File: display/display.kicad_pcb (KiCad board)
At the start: 2 copper layers, 35.8 x 14 mm, 2 parts, among them P1 51281-1694, P2 CONN_14

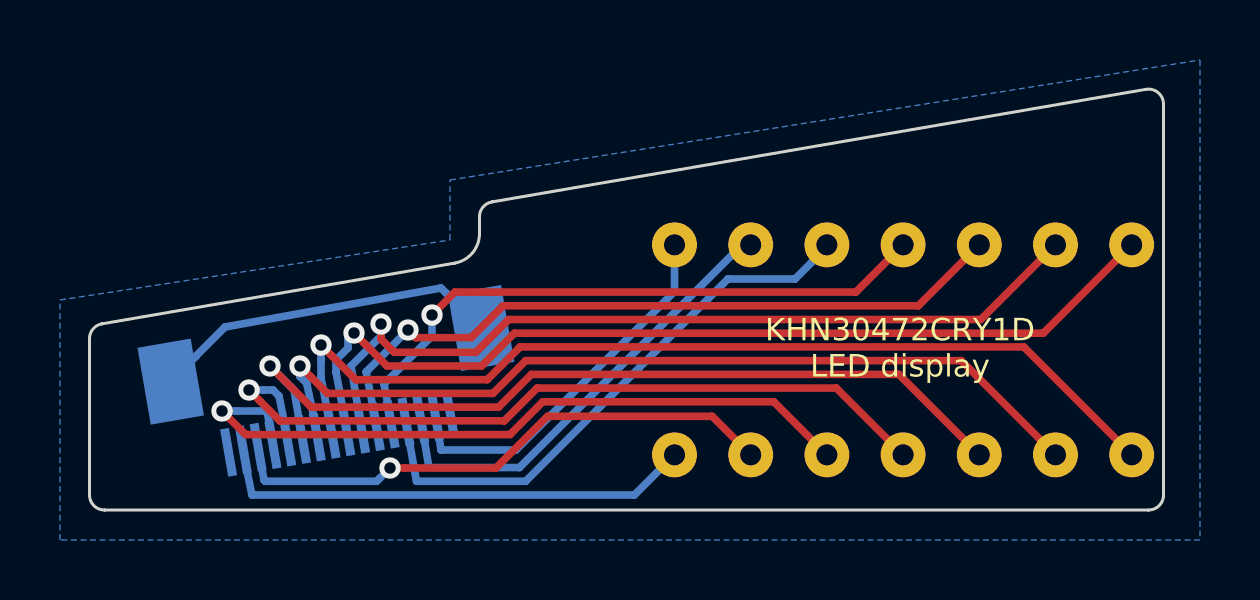
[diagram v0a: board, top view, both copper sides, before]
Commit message: Update FFC connector on the display board.
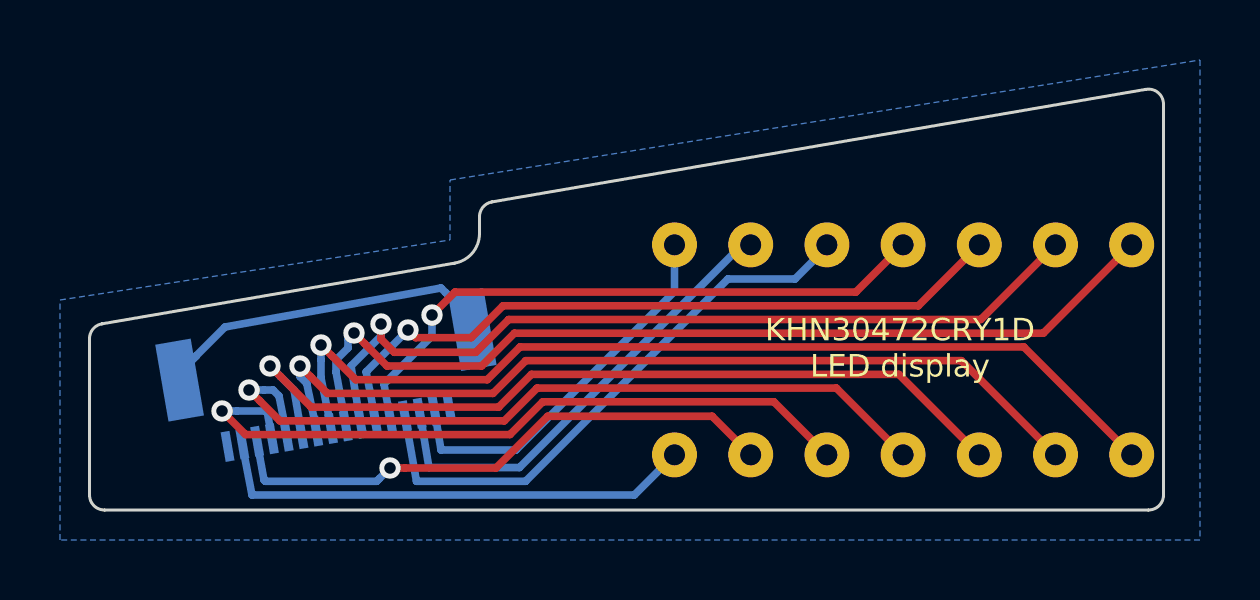
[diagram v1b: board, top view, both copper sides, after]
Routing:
- net /SW9: track 25.0 -> 23.7 mm
- net /CS1: track 33.1 -> 31.8 mm
- net /SW11: track 29.1 -> 28.0 mm
- net /SW7: track 15.5 -> 16.0 mm
- net /CS7: track 15.1 -> 15.6 mm

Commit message: Bump version to 3.1.0
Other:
- board text added: "PCB ID: uhk60v2_display_3.1.0"
- board text removed: "PCB ID: uhk60v2_display_3.0.0"
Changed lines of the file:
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@@
   (title_block
     (title "UHK 60 v2 - LED Display Board")
-    (rev 3.0.0)
+    (rev 3.1.0)
     (company "Ultimate Gadget Laboratories Kft.")
   )
@@
   )
   (setup
-    (last_trace_width 0.254)
+    (last_trace_width 0.3048)
     (user_trace_width 0.2032)
     (user_trace_width 0.254)
@@
   (gr_line (start 135.27385 98.805944) (end 157.073845 95.052999) (angle 90) (layer Edge.Cuts) (width 0.1))
   (gr_arc (start 122.358734 108.576078) (end 121.858673 108.576147) (angle -89.94233769) (layer Edge.Cuts) (width 0.1))
-  (gr_text "PCB ID: uhk60v2_display_3.0.0" (at 157.475 103.775) (layer B.SilkS)
+  (gr_text "PCB ID: uhk60v2_display_3.1.0" (at 157.475 103.775) (layer B.SilkS)
     (effects (font (size 0.75 0.75) (thickness 0.15)) (justify left mirror))
   )

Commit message: Bump version number to 3.2.0
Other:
- board text added: "PCB ID: uhk60v2_display_3.2.0"
- board text removed: "PCB ID: uhk60v2_display_3.1.0"
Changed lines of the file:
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@@
   (title_block
     (title "UHK 60 v2 - LED Display Board")
-    (rev 3.1.0)
+    (rev 3.2.0)
     (company "Ultimate Gadget Laboratories Kft.")
   )
@@
   (gr_line (start 135.27385 98.805944) (end 157.073845 95.052999) (angle 90) (layer Edge.Cuts) (width 0.1))
   (gr_arc (start 122.358734 108.576078) (end 121.858673 108.576147) (angle -89.94233769) (layer Edge.Cuts) (width 0.1))
-  (gr_text "PCB ID: uhk60v2_display_3.1.0" (at 157.475 103.775) (layer B.SilkS)
+  (gr_text "PCB ID: uhk60v2_display_3.2.0" (at 157.475 103.775) (layer B.SilkS)
     (effects (font (size 0.75 0.75) (thickness 0.15)) (justify left mirror))
   )

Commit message: Bump version number to 3.3.0
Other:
- board text added: "PCB ID: uhk60v2_display_3.3.0"
- board text removed: "PCB ID: uhk60v2_display_3.2.0"
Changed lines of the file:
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@@
-(kicad_pcb (version 20171130) (host pcbnew 5.1.5-52549c5~84~ubuntu18.04.1)
+(kicad_pcb (version 20171130) (host pcbnew 5.1.5-52549c5~86~ubuntu18.04.1)
   (general
     (thickness 1.6002)
@@
   (title_block
     (title "UHK 60 v2 - LED Display Board")
-    (rev 3.2.0)
+    (rev 3.3.0)
     (company "Ultimate Gadget Laboratories Kft.")
   )
@@
   (gr_line (start 135.27385 98.805944) (end 157.073845 95.052999) (angle 90) (layer Edge.Cuts) (width 0.1))
   (gr_arc (start 122.358734 108.576078) (end 121.858673 108.576147) (angle -89.94233769) (layer Edge.Cuts) (width 0.1))
-  (gr_text "PCB ID: uhk60v2_display_3.2.0" (at 157.475 103.775) (layer B.SilkS)
+  (gr_text "PCB ID: uhk60v2_display_3.3.0" (at 157.475 103.775) (layer B.SilkS)
     (effects (font (size 0.75 0.75) (thickness 0.15)) (justify left mirror))
   )

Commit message: Bump version to 3.4.0
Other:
- board text added: "PCB ID: uhk60v2_display_3.4.0"
- board text removed: "PCB ID: uhk60v2_display_3.3.0"
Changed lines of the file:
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@@
-(kicad_pcb (version 20171130) (host pcbnew 5.1.5-52549c5~86~ubuntu18.04.1)
+(kicad_pcb (version 20171130) (host pcbnew 5.1.6-c6e7f7d~86~ubuntu18.04.1)
   (general
     (thickness 1.6002)
@@
   (title_block
     (title "UHK 60 v2 - LED Display Board")
-    (rev 3.3.0)
+    (rev 3.4.0)
     (company "Ultimate Gadget Laboratories Kft.")
   )
@@
       (effects (font (size 0.75 0.75) (thickness 0.15)) (justify mirror))
     )
+    (fp_line (start 4.2 3.55) (end 5.05 3.55) (layer B.SilkS) (width 0.15))
+    (fp_line (start 5.05 3.55) (end 5.05 3) (layer B.SilkS) (width 0.15))
+    (fp_line (start -5.05 3.55) (end -5.05 3) (layer B.SilkS) (width 0.15))
+    (fp_line (start -5.05 3.55) (end -4.2 3.55) (layer B.SilkS) (width 0.15))
     (fp_line (start -5.05 0) (end 5.15 0) (layer Margin) (width 0.15))
-    (fp_line (start -5.05 3.55) (end -4.2 3.55) (layer B.SilkS) (width 0.15))
-    (fp_line (start -5.05 3.55) (end -5.05 3) (layer B.SilkS) (width 0.15))
-    (fp_line (start 5.05 3.55) (end 5.05 3) (layer B.SilkS) (width 0.15))
-    (fp_line (start 4.2 3.55) (end 5.05 3.55) (layer B.SilkS) (width 0.15))
     (pad 16 smd rect (at 3.75 4 9.8) (size 0.3 1) (layers B.Cu B.Paste B.Mask)
       (net 1 GND) (clearance 0.1778))
@@
       (effects (font (size 0.75 0.75) (thickness 0.15)))
     )
+    (fp_line (start 34.866338 -11.972218) (end 37.737554 4.453907) (layer Eco1.User) (width 0.1))
+    (fp_line (start 37.245021 5.04) (end -9.66 5.04) (layer Eco1.User) (width 0.1))
+    (fp_line (start -10.16 4.54) (end -10.16 -4.30556) (layer Eco1.User) (width 0.1))
+    (fp_line (start -9.744829 -4.798312) (end 34.288977 -12.378877) (layer Eco1.User) (width 0.1))
+    (fp_line (start 35.34 5.04) (end 35.34 6.34) (layer Eco1.User) (width 0.1))
+    (fp_line (start 33.34 6.34) (end 33.34 5.04) (layer Eco1.User) (width 0.1))
+    (fp_line (start 35.34 6.34) (end 33.34 6.34) (layer Eco1.User) (width 0.1))
+    (fp_line (start -4.66 5.04) (end -4.66 6.34) (layer Eco1.User) (width 0.1))
+    (fp_line (start -6.66 6.34) (end -6.66 5.04) (layer Eco1.User) (width 0.1))
+    (fp_line (start -4.66 6.34) (end -6.66 6.34) (layer Eco1.User) (width 0.1))
+    (fp_line (start -6.398994 -5.879315) (end -6.315017 -5.388765) (layer Eco1.User) (width 0.1))
+    (fp_line (start -8.37 -5.54) (end -6.398994 -5.879315) (layer Eco1.User) (width 0.1))
+    (fp_line (start -8.286023 -5.04945) (end -8.37 -5.54) (layer Eco1.User) (width 0.1))
+    (fp_line (start 15.34 5.04) (end 15.34 6.34) (layer Eco1.User) (width 0.1))
+    (fp_line (start 13.34 6.34) (end 13.34 5.04) (layer Eco1.User) (width 0.1))
+    (fp_line (start 15.34 6.34) (end 13.34 6.34) (layer Eco1.User) (width 0.1))
+    (fp_line (start 33.021006 -12.669315) (end 33.105106 -12.175069) (layer Eco1.User) (width 0.1))
+    (fp_line (start 31.05 -12.33) (end 33.021006 -12.669315) (layer Eco1.User) (width 0.1))
+    (fp_line (start 31.1341 -11.835754) (end 31.05 -12.33) (layer Eco1.User) (width 0.1))
+    (fp_line (start 13.311006 -9.279315) (end 13.395044 -8.781917) (layer Eco1.User) (width 0.1))
+    (fp_line (start 11.34 -8.94) (end 13.311006 -9.279315) (layer Eco1.User) (width 0.1))
     (fp_line (start 11.424038 -8.442602) (end 11.34 -8.94) (layer Eco1.User) (width 0.1))
-    (fp_line (start 11.34 -8.94) (end 13.311006 -9.279315) (layer Eco1.User) (width 0.1))
-    (fp_line (start 13.311006 -9.279315) (end 13.395044 -8.781917) (layer Eco1.User) (width 0.1))
-    (fp_line (start 31.1341 -11.835754) (end 31.05 -12.33) (layer Eco1.User) (width 0.1))
-    (fp_line (start 31.05 -12.33) (end 33.021006 -12.669315) (layer Eco1.User) (width 0.1))
-    (fp_line (start 33.021006 -12.669315) (end 33.105106 -12.175069) (layer Eco1.User) (width 0.1))
-    (fp_line (start 15.34 6.34) (end 13.34 6.34) (layer Eco1.User) (width 0.1))
-    (fp_line (start 13.34 6.34) (end 13.34 5.04) (layer Eco1.User) (width 0.1))
-    (fp_line (start 15.34 5.04) (end 15.34 6.34) (layer Eco1.User) (width 0.1))
-    (fp_line (start -8.286023 -5.04945) (end -8.37 -5.54) (layer Eco1.User) (width 0.1))
-    (fp_line (start -8.37 -5.54) (end -6.398994 -5.879315) (layer Eco1.User) (width 0.1))
-    (fp_line (start -6.398994 -5.879315) (end -6.315017 -5.388765) (layer Eco1.User) (width 0.1))
-    (fp_line (start -4.66 6.34) (end -6.66 6.34) (layer Eco1.User) (width 0.1))
-    (fp_line (start -6.66 6.34) (end -6.66 5.04) (layer Eco1.User) (width 0.1))
-    (fp_line (start -4.66 5.04) (end -4.66 6.34) (layer Eco1.User) (width 0.1))
-    (fp_line (start 35.34 6.34) (end 33.34 6.34) (layer Eco1.User) (width 0.1))
-    (fp_line (start 33.34 6.34) (end 33.34 5.04) (layer Eco1.User) (width 0.1))
-    (fp_line (start 35.34 5.04) (end 35.34 6.34) (layer Eco1.User) (width 0.1))
     (fp_arc (start -9.66 -4.30556) (end -9.744829 -4.798312) (angle -80.2) (layer Eco1.User) (width 0.1))
     (fp_arc (start -9.66 4.54) (end -10.16 4.54) (angle -90) (layer Eco1.User) (width 0.1))
     (fp_arc (start 37.245021 4.54) (end 37.245021 5.04) (angle -99.9) (layer Eco1.User) (width 0.1))
     (fp_arc (start 34.373806 -11.886125) (end 34.866338 -11.972218) (angle -89.8) (layer Eco1.User) (width 0.1))
-    (fp_line (start -9.744829 -4.798312) (end 34.288977 -12.378877) (layer Eco1.User) (width 0.1))
-    (fp_line (start -10.16 4.54) (end -10.16 -4.30556) (layer Eco1.User) (width 0.1))
-    (fp_line (start 37.245021 5.04) (end -9.66 5.04) (layer Eco1.User) (width 0.1))
-    (fp_line (start 34.866338 -11.972218) (end 37.737554 4.453907) (layer Eco1.User) (width 0.1))
     (pad 8 thru_hole circle (at 10.58 -3.5) (size 1.5 1.5) (drill 0.7) (layers *.Cu *.Mask)
       (net 15 /CS2))
@@
   (gr_line (start 135.27385 98.805944) (end 157.073845 95.052999) (angle 90) (layer Edge.Cuts) (width 0.1))
   (gr_arc (start 122.358734 108.576078) (end 121.858673 108.576147) (angle -89.94233769) (layer Edge.Cuts) (width 0.1))
-  (gr_text "PCB ID: uhk60v2_display_3.3.0" (at 157.475 103.775) (layer B.SilkS)
+  (gr_text "PCB ID: uhk60v2_display_3.4.0" (at 157.475 103.775) (layer B.SilkS)
     (effects (font (size 0.75 0.75) (thickness 0.15)) (justify left mirror))
   )
